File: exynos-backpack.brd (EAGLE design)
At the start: 29 x 52 mm, 16 parts, among them IC1 TXB0108RGY, IC2 MIC5335-SPYMT

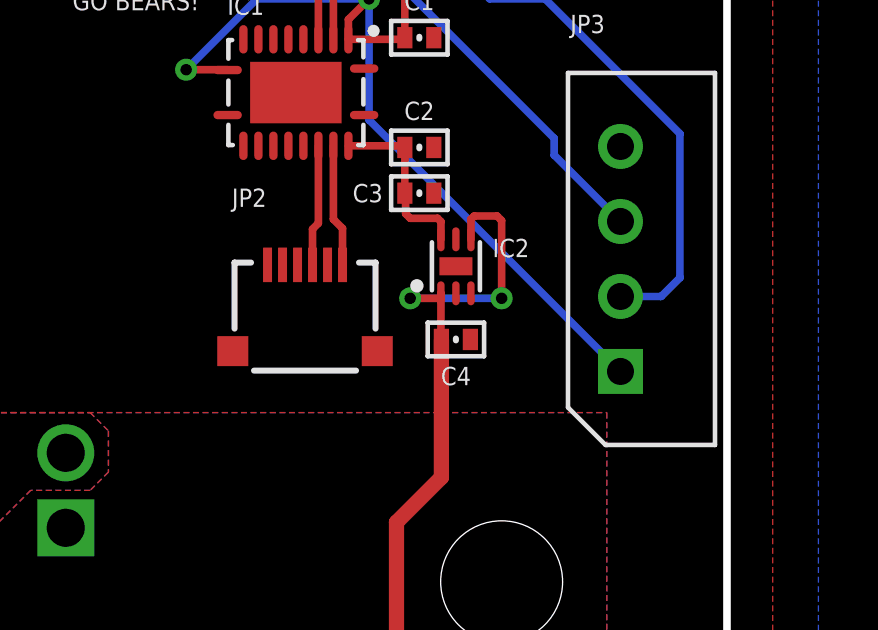
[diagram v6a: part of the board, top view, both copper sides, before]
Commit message: Fix via overlap with silk
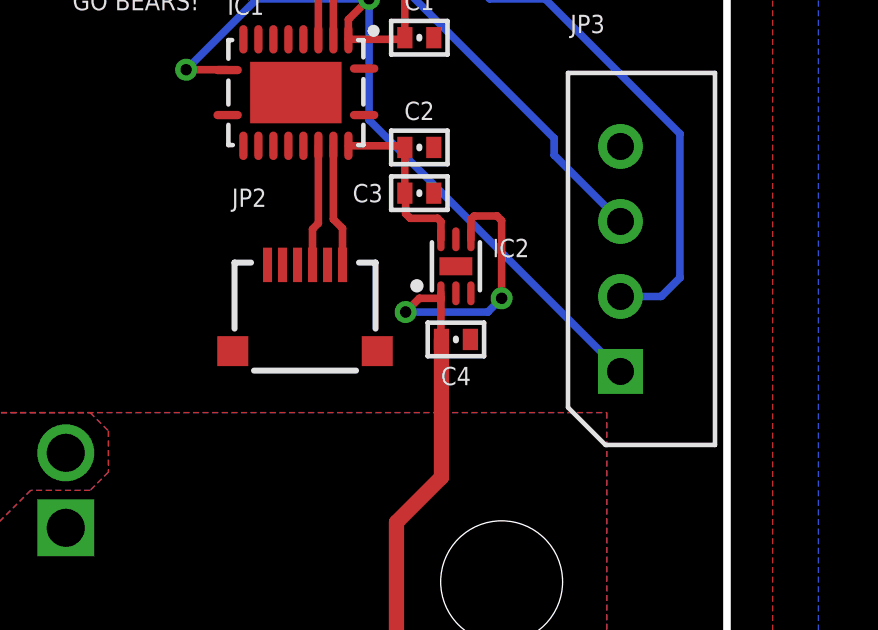
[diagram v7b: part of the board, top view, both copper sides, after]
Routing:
- net V_BATT: track 29.2 -> 29.7 mm
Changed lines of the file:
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@@
 <grid distance="6" unitdist="mil" unit="inch" style="lines" multiple="1" display="yes" altdistance="1" altunitdist="mil" altunit="mil"/>
 <layers>
-<layer number="1" name="Top" color="4" fill="1" visible="no" active="yes"/>
+<layer number="1" name="Top" color="4" fill="1" visible="yes" active="yes"/>
 <layer number="2" name="Route2" color="1" fill="3" visible="no" active="yes"/>
 <layer number="3" name="Route3" color="4" fill="3" visible="no" active="yes"/>
@@
 <layer number="14" name="Route14" color="1" fill="6" visible="no" active="no"/>
 <layer number="15" name="Route15" color="4" fill="6" visible="no" active="no"/>
-<layer number="16" name="Bottom" color="1" fill="1" visible="no" active="yes"/>
+<layer number="16" name="Bottom" color="1" fill="1" visible="yes" active="yes"/>
 <layer number="17" name="Pads" color="2" fill="1" visible="no" active="yes"/>
-<layer number="18" name="Vias" color="2" fill="1" visible="no" active="yes"/>
+<layer number="18" name="Vias" color="2" fill="1" visible="yes" active="yes"/>
 <layer number="19" name="Unrouted" color="6" fill="1" visible="no" active="yes"/>
 <layer number="20" name="Dimension" color="15" fill="1" visible="yes" active="yes"/>
@@
 <contactref element="PS1" pad="2"/>
 <contactref element="JP5" pad="2"/>
-<wire x1="19.4644" y1="35.5236" x2="19.4644" y2="34.0026" width="0.254" layer="1"/>
+<wire x1="19.4644" y1="35.3568" x2="19.4644" y2="34.0026" width="0.254" layer="1"/>
 <wire x1="19.4644" y1="34.0026" x2="19.4818" y2="33.9852" width="0.254" layer="1"/>
 <wire x1="19.4818" y1="33.9852" x2="19.4818" y2="29.3878" width="0.508" layer="1"/>
@@
 <wire x1="21.336" y1="38.1" x2="21.4884" y2="37.9476" width="0.254" layer="1"/>
 <wire x1="21.4884" y1="37.9476" x2="21.4884" y2="35.3568" width="0.254" layer="1"/>
-<via x="18.4404" y="35.3568" extent="1-16" drill="0.381"/>
-<wire x1="21.4884" y1="35.3568" x2="18.4404" y2="35.3568" width="0.254" layer="16"/>
+<via x="18.288" y="34.8996" extent="1-16" drill="0.381"/>
+<wire x1="21.4884" y1="35.3568" x2="21.0312" y2="34.8996" width="0.254" layer="16"/>
+<wire x1="21.0312" y1="34.8996" x2="18.288" y2="34.8996" width="0.254" layer="16"/>
 <wire x1="19.4644" y1="35.5236" x2="19.4644" y2="35.3568" width="0.254" layer="1"/>
-<wire x1="19.4644" y1="35.3568" x2="18.4404" y2="35.3568" width="0.254" layer="1"/>
+<wire x1="19.4644" y1="35.3568" x2="18.7452" y2="35.3568" width="0.254" layer="1"/>
+<wire x1="18.7452" y1="35.3568" x2="18.288" y2="34.8996" width="0.254" layer="1"/>
 </signal>
 <signal name="3.3V">
